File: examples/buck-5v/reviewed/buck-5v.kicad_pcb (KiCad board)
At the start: 2 copper layers, 126 x 56 mm, 11 parts, among them J1 12V IN, J2 5V OUT, U1 LM2596S-5

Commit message: Regenerate the five with stitched pours, silk that speaks, and wires that never double back
All ten variants rebuilt by the fixed generator: reviewed boards carry
ground on both faces with the stitching ring (buck 35 vias, fpga 116),
thru_hole_only front pours, the board id and connector pin names in
silk, and the buck's explicit ground return; the sheets hook power up
through upright symbols and source-anchored flags with no overlapping
wires and no junction-less tees left. Every reviewed variant passes its
own gate with zero errors; every as-generated variant still fails, now
also for the rules this round added.

Co-Authored-By: Claude Fable 5 <noreply@anthropic.com>
Claude-Session: https://claude.ai/code/session_01DUj7Ltu92tWg159mCSacwY
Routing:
- net GND: track 107.8 -> 201.8 mm, vias 11 -> 35
- added copper zone on F.Cu, net GND
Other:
- board text added: "+12V"
- board text added: "+5V"
- board text added: "5V OK"
- board text added: "GND"
- board text added: "buck-5v rev A"
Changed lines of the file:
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@@
 	(segment (start 221.0 96.0) (end 221.0 110.0) (width 1.0) (layer "F.Cu") (net 1))
 	(segment (start 221.0 110.0) (end 210.0 110.0) (width 1.0) (layer "F.Cu") (net 1))
+	(segment (start 116.0 110.0) (end 210.0 110.0) (width 1.0) (layer "F.Cu") (net 1))
 	(segment (start 154.35 72.0) (end 151.0 72.0) (width 1.0) (layer "F.Cu") (net 1))
 	(segment (start 154.35 75.4) (end 154.35 80.0) (width 1.0) (layer "F.Cu") (net 1))
@@
 	(via (at 203.7 98.6) (size 0.8) (drill 0.4) (layers "F.Cu" "B.Cu") (net 1))
 	(via (at 207.938 110.0) (size 0.8) (drill 0.4) (layers "F.Cu" "B.Cu") (net 1))
+	(via (at 116.5 112.5) (size 0.8) (drill 0.4) (layers "F.Cu" "B.Cu") (net 1))
+	(via (at 126.5 112.5) (size 0.8) (drill 0.4) (layers "F.Cu" "B.Cu") (net 1))
+	(via (at 136.5 112.5) (size 0.8) (drill 0.4) (layers "F.Cu" "B.Cu") (net 1))
+	(via (at 146.5 112.5) (size 0.8) (drill 0.4) (layers "F.Cu" "B.Cu") (net 1))
+	(via (at 156.5 63.5) (size 0.8) (drill 0.4) (layers "F.Cu" "B.Cu") (net 1))
+	(via (at 156.5 112.5) (size 0.8) (drill 0.4) (layers "F.Cu" "B.Cu") (net 1))
+	(via (at 166.5 63.5) (size 0.8) (drill 0.4) (layers "F.Cu" "B.Cu") (net 1))
+	(via (at 166.5 112.5) (size 0.8) (drill 0.4) (layers "F.Cu" "B.Cu") (net 1))
+	(via (at 176.5 63.5) (size 0.8) (drill 0.4) (layers "F.Cu" "B.Cu") (net 1))
+	(via (at 176.5 112.5) (size 0.8) (drill 0.4) (layers "F.Cu" "B.Cu") (net 1))
+	(via (at 186.5 63.5) (size 0.8) (drill 0.4) (layers "F.Cu" "B.Cu") (net 1))
+	(via (at 186.5 112.5) (size 0.8) (drill 0.4) (layers "F.Cu" "B.Cu") (net 1))
+	(via (at 196.5 63.5) (size 0.8) (drill 0.4) (layers "F.Cu" "B.Cu") (net 1))
+	(via (at 196.5 112.5) (size 0.8) (drill 0.4) (layers "F.Cu" "B.Cu") (net 1))
+	(via (at 206.5 63.5) (size 0.8) (drill 0.4) (layers "F.Cu" "B.Cu") (net 1))
+	(via (at 206.5 112.5) (size 0.8) (drill 0.4) (layers "F.Cu" "B.Cu") (net 1))
+	(via (at 116.5 73.5) (size 0.8) (drill 0.4) (layers "F.Cu" "B.Cu") (net 1))
+	(via (at 210.5 73.5) (size 0.8) (drill 0.4) (layers "F.Cu" "B.Cu") (net 1))
+	(via (at 116.5 83.5) (size 0.8) (drill 0.4) (layers "F.Cu" "B.Cu") (net 1))
+	(via (at 210.5 83.5) (size 0.8) (drill 0.4) (layers "F.Cu" "B.Cu") (net 1))
+	(via (at 116.5 93.5) (size 0.8) (drill 0.4) (layers "F.Cu" "B.Cu") (net 1))
+	(via (at 210.5 93.5) (size 0.8) (drill 0.4) (layers "F.Cu" "B.Cu") (net 1))
+	(via (at 116.5 103.5) (size 0.8) (drill 0.4) (layers "F.Cu" "B.Cu") (net 1))
+	(via (at 210.5 103.5) (size 0.8) (drill 0.4) (layers "F.Cu" "B.Cu") (net 1))
 	(zone
 		(net 1)
@@
 		(polygon (pts (xy 115.0 62.0) (xy 212.0 62.0) (xy 212.0 114.0) (xy 115.0 114.0)))
 	)
+	(zone
+		(net 1)
+		(net_name "GND")
+		(layer "F.Cu")
+		(hatch edge 0.5)
+		(connect_pads thru_hole_only
+			(clearance 0.4)
+		)
+		(min_thickness 0.175)
+		(filled_areas_thickness no)
+		(fill yes
+			(thermal_gap 0.5)
+			(thermal_bridge_width 0.5)
+		)
+		(polygon (pts (xy 115.0 62.0) (xy 212.0 62.0) (xy 212.0 114.0) (xy 115.0 114.0)))
+	)
+	(gr_text "buck-5v rev A" (at 163.0 113.8 0) (layer "F.SilkS") (effects (font (size 1.0 1.0) (thickness 0.15))))
+	(gr_text "+12V" (at 110.0 78.91 0) (layer "F.SilkS") (effects (font (size 0.8 0.8) (thickness 0.12))))
+	(gr_text "GND" (at 105.0 78.91 0) (layer "F.SilkS") (effects (font (size 0.8 0.8) (thickness 0.12))))
+	(gr_text "5V OK" (at 207.0 103.4 0) (layer "F.SilkS") (effects (font (size 0.8 0.8) (thickness 0.12))))
+	(gr_text "+5V" (at 216.0 89.09 0) (layer "F.SilkS") (effects (font (size 0.8 0.8) (thickness 0.12))))
+	(gr_text "GND" (at 221.0 89.09 0) (layer "F.SilkS") (effects (font (size 0.8 0.8) (thickness 0.12))))
 )

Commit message: Regenerate the five as round three drew them
All five reviewed projects pass their gates again: the buck all wire
with its feedback drawn home, the motor's logic named at the header,
the carrier reading as the pinout table it is - with its feed diode
finally pointing the right way - the filter compact with test points,
and the FPGA's capacitors sitting beside the units they feed. Thirty
renders redrawn, verdict tables at today's numbers.

Co-Authored-By: Claude Fable 5 <noreply@anthropic.com>
Claude-Session: https://claude.ai/code/session_01DUj7Ltu92tWg159mCSacwY
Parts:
- turned J1 to 270 degrees
- turned J2 to 90 degrees
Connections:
- net +12V renamed /+12V
- net +5V renamed /+5V
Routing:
- net GND: track 201.8 -> 197.1 mm, vias 35 -> 46
- net /SW: track 79.1 -> 75.6 mm
- net /+12V: track 64.9 -> 61.9 mm
- net /+5V: track 136.5 -> 138.1 mm
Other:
- board text added: "kicad_skills examples"

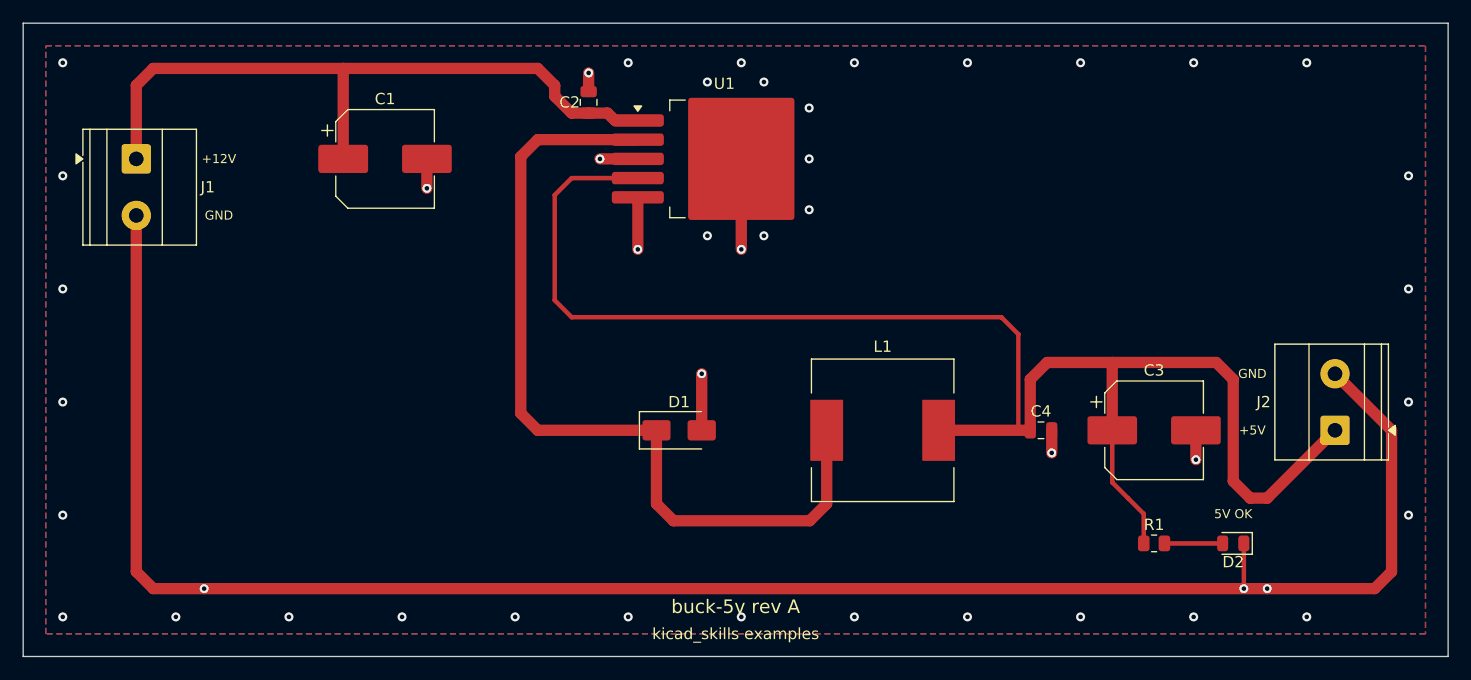
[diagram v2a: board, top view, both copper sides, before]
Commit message: Regenerate the four boards round four has settled
The buck, the motor driver, the carrier and the filter as the current
generator draws them: interior ground stitching on all four, the motor
driver's bundle tight and its board twelve millimetres shorter, the
filter compact and hand-placed, the carrier's indicator in a column of
its own. All four pass their gates. The FPGA is still regenerating.

Co-Authored-By: Claude Fable 5 <noreply@anthropic.com>
Claude-Session: https://claude.ai/code/session_01DUj7Ltu92tWg159mCSacwY
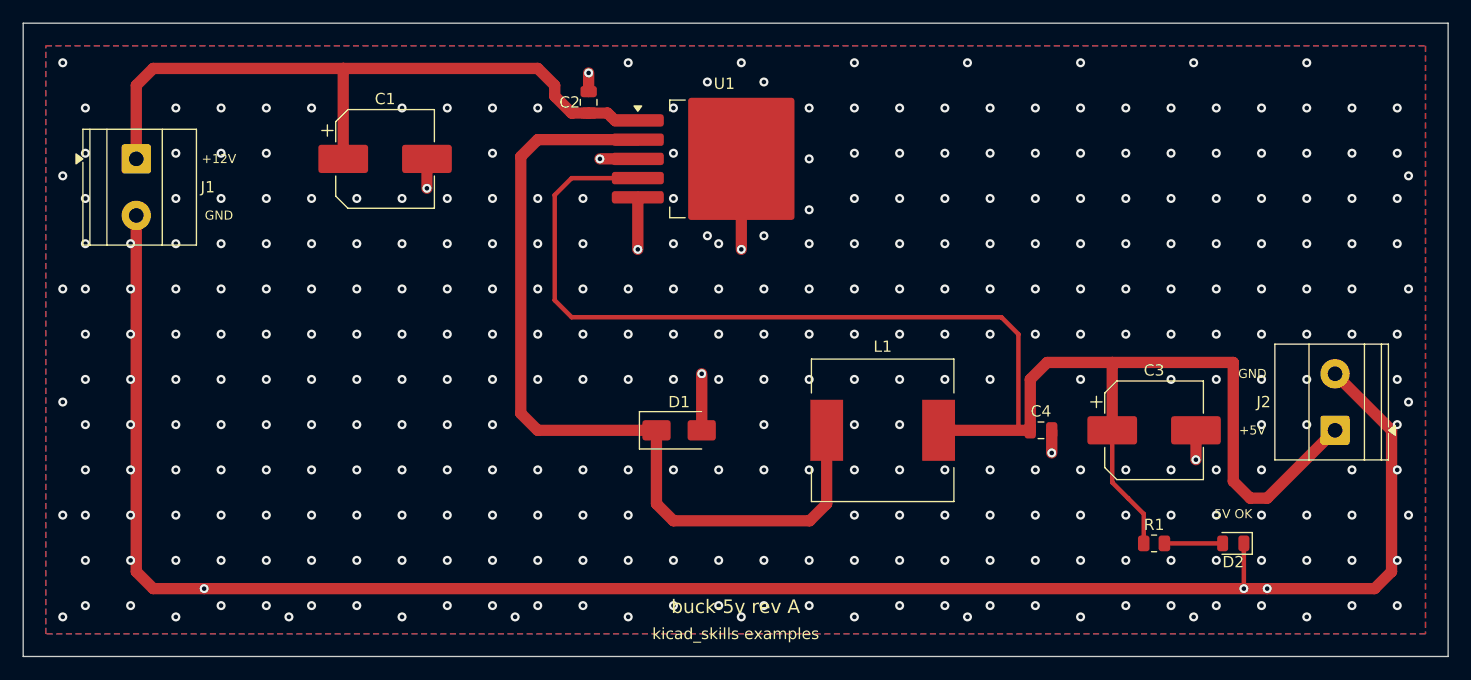
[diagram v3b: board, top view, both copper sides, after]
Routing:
- net /+5V: track 138.1 -> 138.9 mm
- net GND: vias 46 -> 351

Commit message: Regenerate the four boards whose corners were off the grid
Ninety-one bends at angles nobody chose, now none. All four still pass
their gates.

Co-Authored-By: Claude Fable 5 <noreply@anthropic.com>
Claude-Session: https://claude.ai/code/session_01DUj7Ltu92tWg159mCSacwY
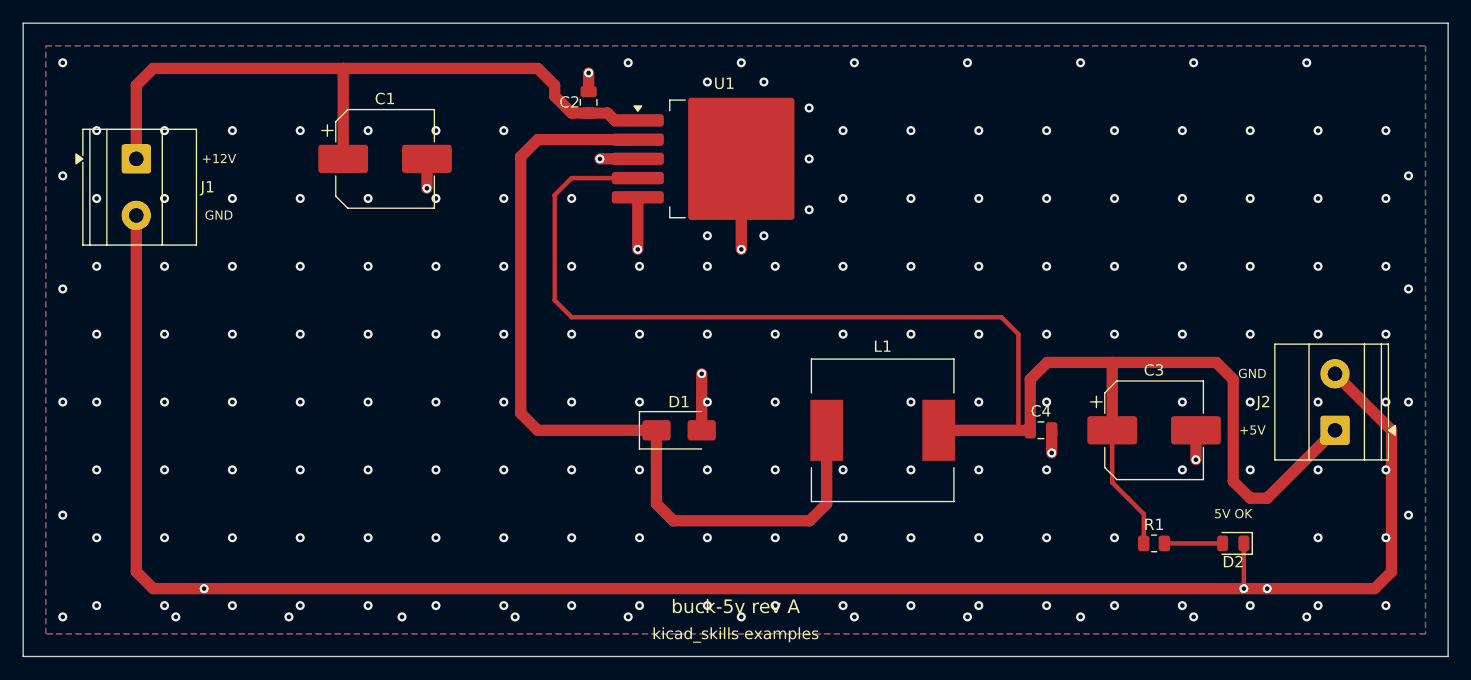
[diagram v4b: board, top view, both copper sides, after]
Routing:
- net /+5V: track 138.9 -> 138.1 mm
- net GND: vias 351 -> 194

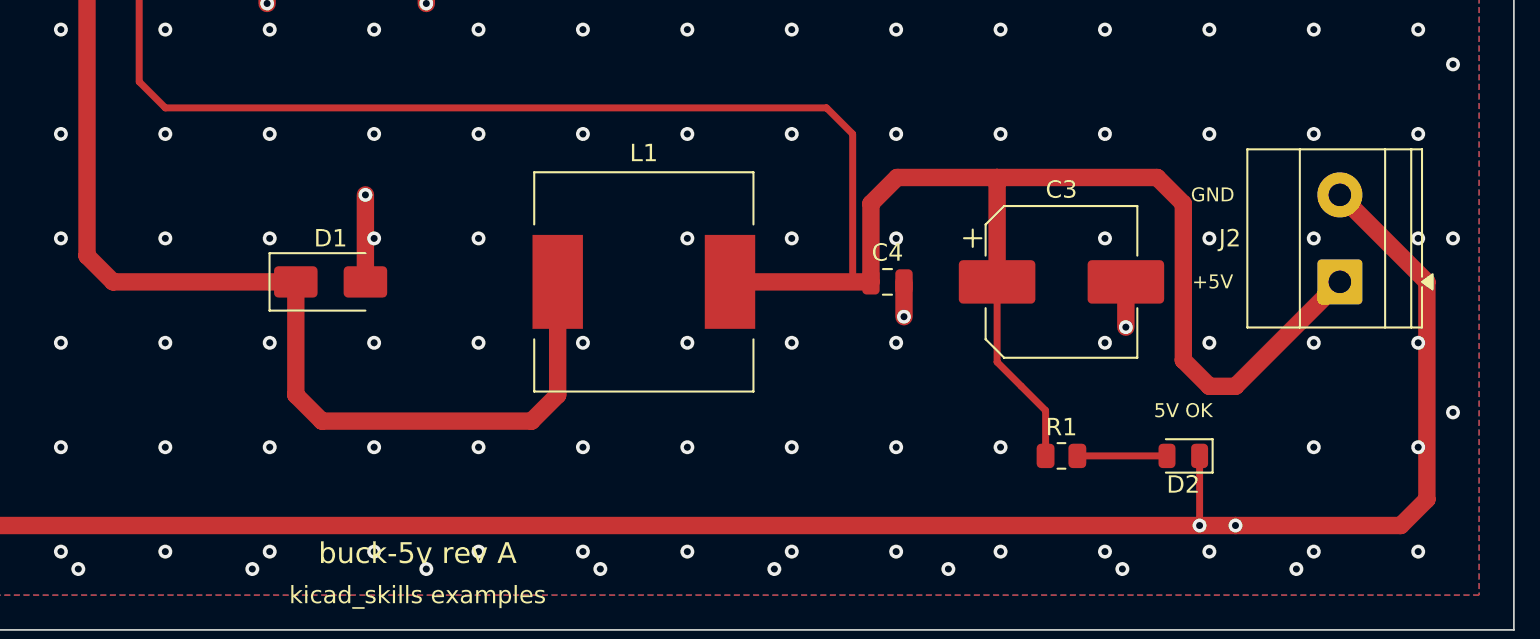
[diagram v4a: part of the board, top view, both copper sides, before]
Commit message: Regenerate the four the text and width work changed
Designators and values off the rails they were printed on, power-named
nets at the width their rule asks for, and the buck's feedback ending
on the capacitor pad it senses at.

Co-Authored-By: Claude Fable 5 <noreply@anthropic.com>
Claude-Session: https://claude.ai/code/session_01DUj7Ltu92tWg159mCSacwY
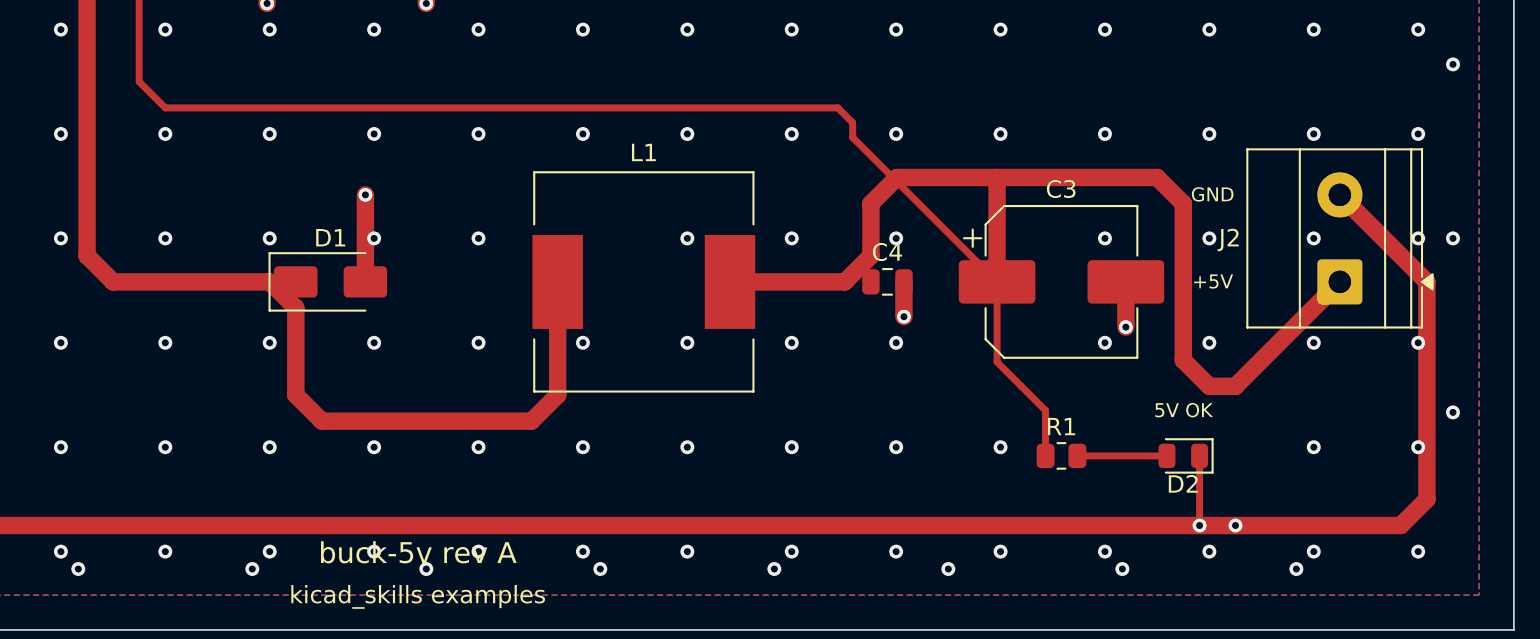
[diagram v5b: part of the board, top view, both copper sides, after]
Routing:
- net /+5V: track 138.1 -> 141.0 mm
- net /SW: track 75.6 -> 74.7 mm
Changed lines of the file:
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@@
 	(segment (start 144.0 71.8) (end 144.0 94.5) (width 1.0) (layer "F.Cu") (net 5))
 	(segment (start 144.0 94.5) (end 145.5 96.0) (width 1.0) (layer "F.Cu") (net 5))
-	(segment (start 145.5 96.0) (end 156.0 96.0) (width 1.0) (layer "F.Cu") (net 5))
-	(segment (start 156.0 96.0) (end 156.0 102.5) (width 1.0) (layer "F.Cu") (net 5))
+	(segment (start 145.5 96.0) (end 154.5 96.0) (width 1.0) (layer "F.Cu") (net 5))
+	(segment (start 154.5 96.0) (end 156.0 97.5) (width 1.0) (layer "F.Cu") (net 5))
+	(segment (start 156.0 97.5) (end 156.0 102.5) (width 1.0) (layer "F.Cu") (net 5))
 	(segment (start 156.0 102.5) (end 157.5 104.0) (width 1.0) (layer "F.Cu") (net 5))
 	(segment (start 157.5 104.0) (end 169.55 104.0) (width 1.0) (layer "F.Cu") (net 5))
@@
 	(segment (start 147.0 75.2) (end 147.0 84.5) (width 0.4) (layer "F.Cu") (net 3))
 	(segment (start 147.0 84.5) (end 148.5 86.0) (width 0.4) (layer "F.Cu") (net 3))
-	(segment (start 148.5 86.0) (end 186.5 86.0) (width 0.4) (layer "F.Cu") (net 3))
-	(segment (start 186.5 86.0) (end 188.0 87.5) (width 0.4) (layer "F.Cu") (net 3))
-	(segment (start 188.0 87.5) (end 188.0 96.0) (width 0.4) (layer "F.Cu") (net 3))
-	(segment (start 180.95 96.0) (end 189.05 96.0) (width 1.0) (layer "F.Cu") (net 3))
-	(segment (start 189.05 96.0) (end 189.05 91.5) (width 1.0) (layer "F.Cu") (net 3))
+	(segment (start 148.5 86.0) (end 187.15 86.0) (width 0.4) (layer "F.Cu") (net 3))
+	(segment (start 187.15 86.0) (end 188.0 86.85) (width 0.4) (layer "F.Cu") (net 3))
+	(segment (start 188.0 86.85) (end 188.0 87.7) (width 0.4) (layer "F.Cu") (net 3))
+	(segment (start 188.0 87.7) (end 196.3 96.0) (width 0.4) (layer "F.Cu") (net 3))
+	(segment (start 180.95 96.0) (end 187.55 96.0) (width 1.0) (layer "F.Cu") (net 3))
+	(segment (start 187.55 96.0) (end 189.05 94.5) (width 1.0) (layer "F.Cu") (net 3))
+	(segment (start 189.05 94.5) (end 189.05 91.5) (width 1.0) (layer "F.Cu") (net 3))
 	(segment (start 189.05 91.5) (end 190.55 90.0) (width 1.0) (layer "F.Cu") (net 3))
 	(segment (start 190.55 90.0) (end 196.3 90.0) (width 1.0) (layer "F.Cu") (net 3))
@@
 	(segment (start 110.0 108.5) (end 111.5 110.0) (width 1.0) (layer "F.Cu") (net 1))
 	(segment (start 111.5 110.0) (end 116.0 110.0) (width 1.0) (layer "F.Cu") (net 1))
-	(segment (start 216.0 91.0) (end 221.0 96.0) (width 1.0) (layer "F.Cu") (net 1))
-	(segment (start 221.0 96.0) (end 221.0 108.5) (width 1.0) (layer "F.Cu") (net 1))
-	(segment (start 221.0 108.5) (end 219.5 110.0) (width 1.0) (layer "F.Cu") (net 1))
-	(segment (start 219.5 110.0) (end 210.0 110.0) (width 1.0) (layer "F.Cu") (net 1))
 	(segment (start 116.0 110.0) (end 210.0 110.0) (width 1.0) (layer "F.Cu") (net 1))
+	(segment (start 210.0 110.0) (end 219.5 110.0) (width 1.0) (layer "F.Cu") (net 1))
+	(segment (start 219.5 110.0) (end 221.0 108.5) (width 1.0) (layer "F.Cu") (net 1))
+	(segment (start 221.0 108.5) (end 221.0 96.0) (width 1.0) (layer "F.Cu") (net 1))
+	(segment (start 221.0 96.0) (end 216.0 91.0) (width 1.0) (layer "F.Cu") (net 1))
 	(segment (start 154.35 72.0) (end 151.0 72.0) (width 1.0) (layer "F.Cu") (net 1))
 	(segment (start 154.35 75.4) (end 154.35 80.0) (width 1.0) (layer "F.Cu") (net 1))
@@
 	(via (at 178.5 87.5) (size 0.8) (drill 0.4) (layers "F.Cu" "B.Cu") (net 1))
 	(via (at 184.5 87.5) (size 0.8) (drill 0.4) (layers "F.Cu" "B.Cu") (net 1))
-	(via (at 190.5 87.5) (size 0.8) (drill 0.4) (layers "F.Cu" "B.Cu") (net 1))
 	(via (at 196.5 87.5) (size 0.8) (drill 0.4) (layers "F.Cu" "B.Cu") (net 1))
 	(via (at 202.5 87.5) (size 0.8) (drill 0.4) (layers "F.Cu" "B.Cu") (net 1))
@@
 	(via (at 214.5 111.5) (size 0.8) (drill 0.4) (layers "F.Cu" "B.Cu") (net 1))
 	(via (at 220.5 111.5) (size 0.8) (drill 0.4) (layers "F.Cu" "B.Cu") (net 1))
+	(via (at 190.5 87.5) (size 0.8) (drill 0.4) (layers "F.Cu" "B.Cu") (net 1))
 	(zone
 		(net 1)
